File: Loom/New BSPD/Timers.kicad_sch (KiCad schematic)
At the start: 4 parts, among them U13 4081, U8 4040, U9 4040

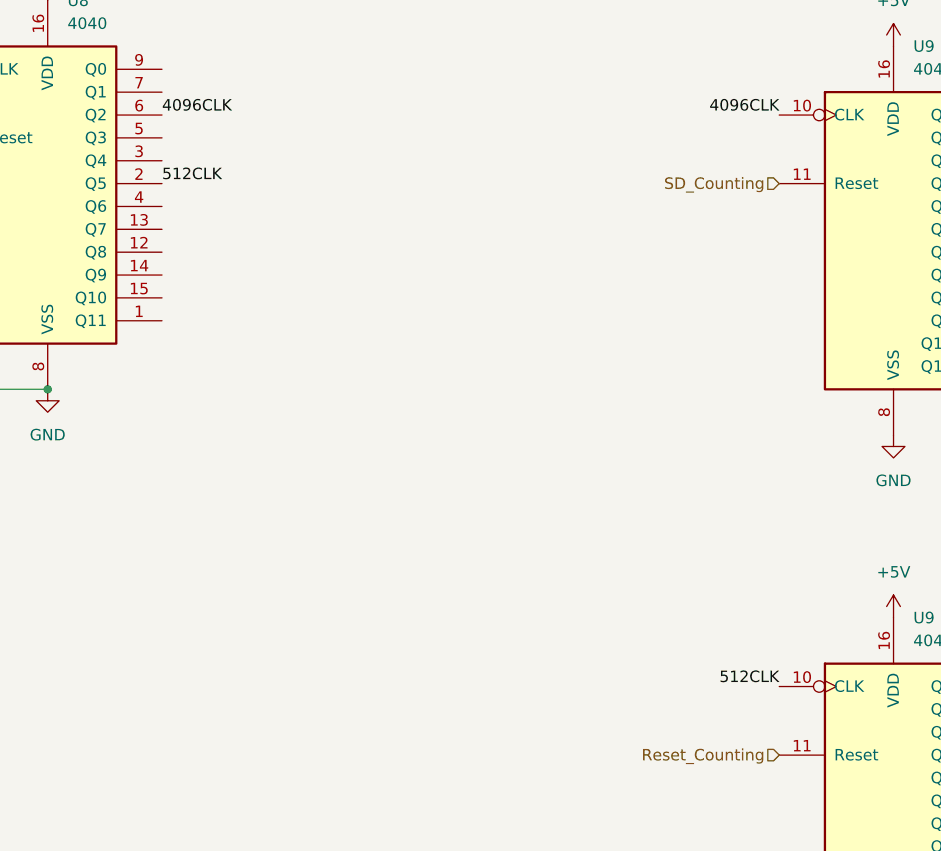
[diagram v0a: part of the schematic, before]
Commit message: Fix BSPD Timing
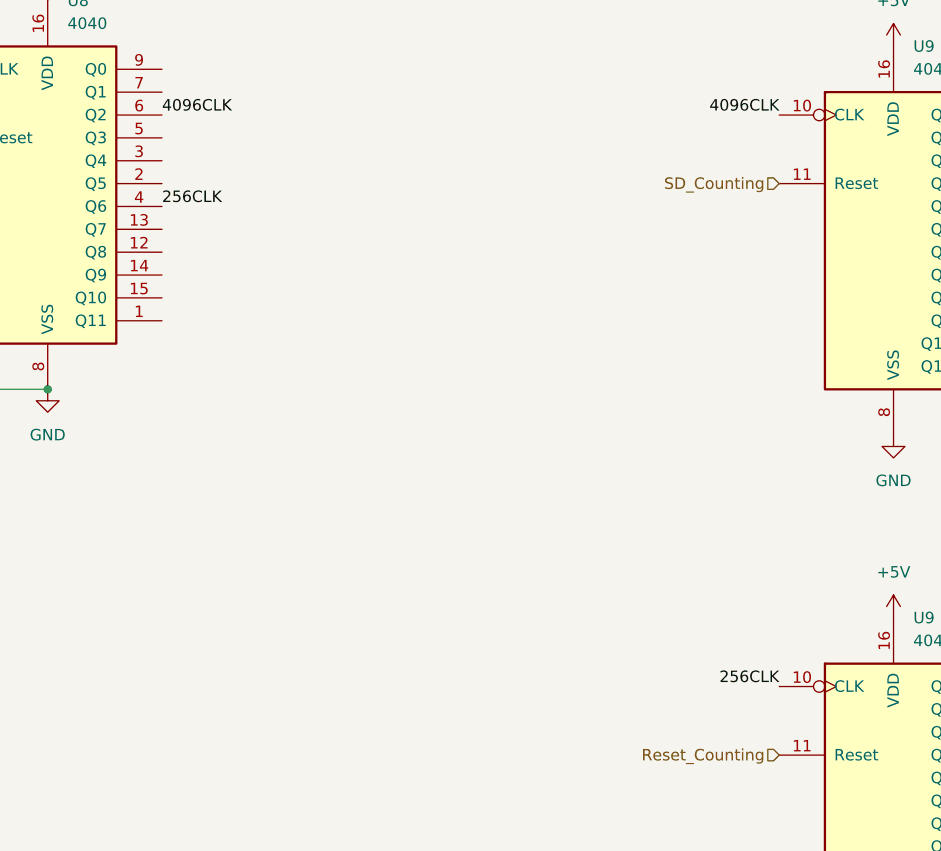
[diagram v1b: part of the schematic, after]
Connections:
- net 256CLK: now reaches U8.4 (Q6)
- net 256CLK: now also U9.10 (CLK)
- net 512CLK: no longer names the net of U8.2 (Q5)
- net 512CLK: no longer U9.10 (CLK)
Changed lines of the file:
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@@
     (effects (font (size 1.27 1.27)) (justify right bottom))
   )
-  (label "512CLK" (at 119.38 99.06 180) (fields_autoplaced)
+  (label "256CLK" (at 119.38 99.06 180) (fields_autoplaced)
     (effects (font (size 1.27 1.27)) (justify right bottom))
   )
-  (label "512CLK" (at 50.8 43.18 0) (fields_autoplaced)
+  (label "256CLK" (at 50.8 45.72 0) (fields_autoplaced)
     (effects (font (size 1.27 1.27)) (justify left bottom))
   )

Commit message: Complete BSPD Schematic
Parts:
- removed U13: 4081, symbol 4xxx:4081
- added U6: 4011, symbol 4xxx:4011
- renumbered U8 to U?, U9 to U?
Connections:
- net 10s_Timer: now also U6.11
- net at U?.1 (Q11): now also U6.9
- net at U?.14 (Q9): now also U6.8
- new net: U6.10, U6.12, U6.13
- no-connect marks 0 -> 31

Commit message: Complete Schematic, Footprint Assignment, Start PCB Design
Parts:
- U6: footprint (none) -> Package_DIP:DIP-14_W7.62mm_Socket
- U? (x3): footprint (none) -> Package_DIP:DIP-16_W7.62mm_Socket
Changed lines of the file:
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@@
       (effects (font (size 1.27 1.27)))
     )
-    (property "Footprint" "" (at 153.67 124.46 0)
+    (property "Footprint" "Package_DIP:DIP-14_W7.62mm_Socket" (at 153.67 124.46 0)
       (effects (font (size 1.27 1.27)) hide)
     )
@@
       (effects (font (size 1.27 1.27)) (justify left))
     )
-    (property "Footprint" "" (at 38.1 43.18 0)
+    (property "Footprint" "Package_DIP:DIP-16_W7.62mm_Socket" (at 38.1 43.18 0)
       (effects (font (size 1.27 1.27)) hide)
     )
@@
       (effects (font (size 1.27 1.27)) (justify left))
     )
-    (property "Footprint" "" (at 132.08 111.76 0)
+    (property "Footprint" "Package_DIP:DIP-16_W7.62mm_Socket" (at 132.08 111.76 0)
       (effects (font (size 1.27 1.27)) hide)
     )
@@
       (effects (font (size 1.27 1.27)) (justify left))
     )
-    (property "Footprint" "" (at 132.08 48.26 0)
+    (property "Footprint" "Package_DIP:DIP-16_W7.62mm_Socket" (at 132.08 48.26 0)
       (effects (font (size 1.27 1.27)) hide)
     )
@@
       (effects (font (size 1.27 1.27)))
     )
-    (property "Footprint" "" (at 170.18 124.46 0)
-      (effects (font (size 1.27 1.27)) hide)
-    )
+    (property "Footprint" "Package_DIP:DIP-14_W7.62mm_Socket" (at 170.18 124.46 0)
+      (effects (font (size 1.27 1.27)) hide)
+    )
